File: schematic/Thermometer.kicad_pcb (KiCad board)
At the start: 2 copper layers, 55.4 x 52.8 mm, 18 parts, among them Q1 BC547, Q2 BC547, Q3 BC547, Q4 BC547, SW1 SW_SPDT, U1 CC56-12EWA, U2 DS18B20, U3 DS18B20

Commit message: Updated Schematic and PCB with (hopefully) final designs
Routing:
- net Net-(Q3-B): track 53.3 -> 77.8 mm, vias 2 -> 3
- net Net-(SW1-C): track 96.7 -> 115.0 mm, vias 1 -> 2
- net Net-(Q2-B): track 74.0 -> 57.0 mm, vias 2 -> 1
- net Net-(Q1-E): track 51.7 -> 42.5 mm
- net Net-(A1-A1): track 67.0 -> 59.1 mm
- net Net-(A1-D11): track 47.8 -> 54.9 mm
- net Net-(Q3-C): track 55.3 -> 48.4 mm
- net Net-(A1-D9): track 45.7 -> 50.8 mm
- net Net-(A1-D2): track 27.5 -> 22.6 mm
- net Net-(A1-D12): track 42.7 -> 47.3 mm
- net Net-(Q2-C): track 39.9 -> 44.1 mm
- net Net-(A1-+5V): track 85.7 -> 82.3 mm, vias 0 -> 1
- net Net-(D1-K): track 48.3 -> 51.6 mm
- net Net-(A1-D3): track 24.7 -> 21.9 mm, vias 0 -> 1
- net Net-(U2-DQ): track 34.4 -> 36.5 mm, vias 0 -> 1
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
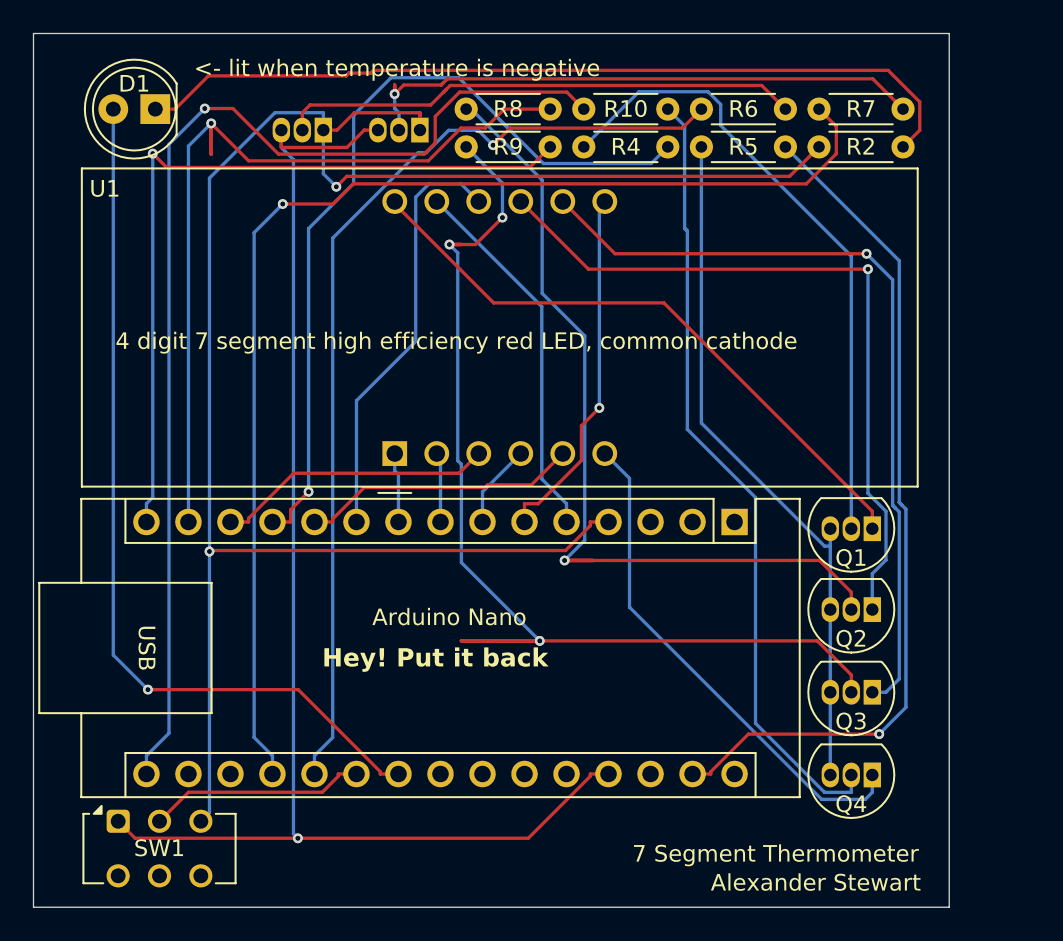
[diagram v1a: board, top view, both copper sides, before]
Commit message: Updated error in PCB design
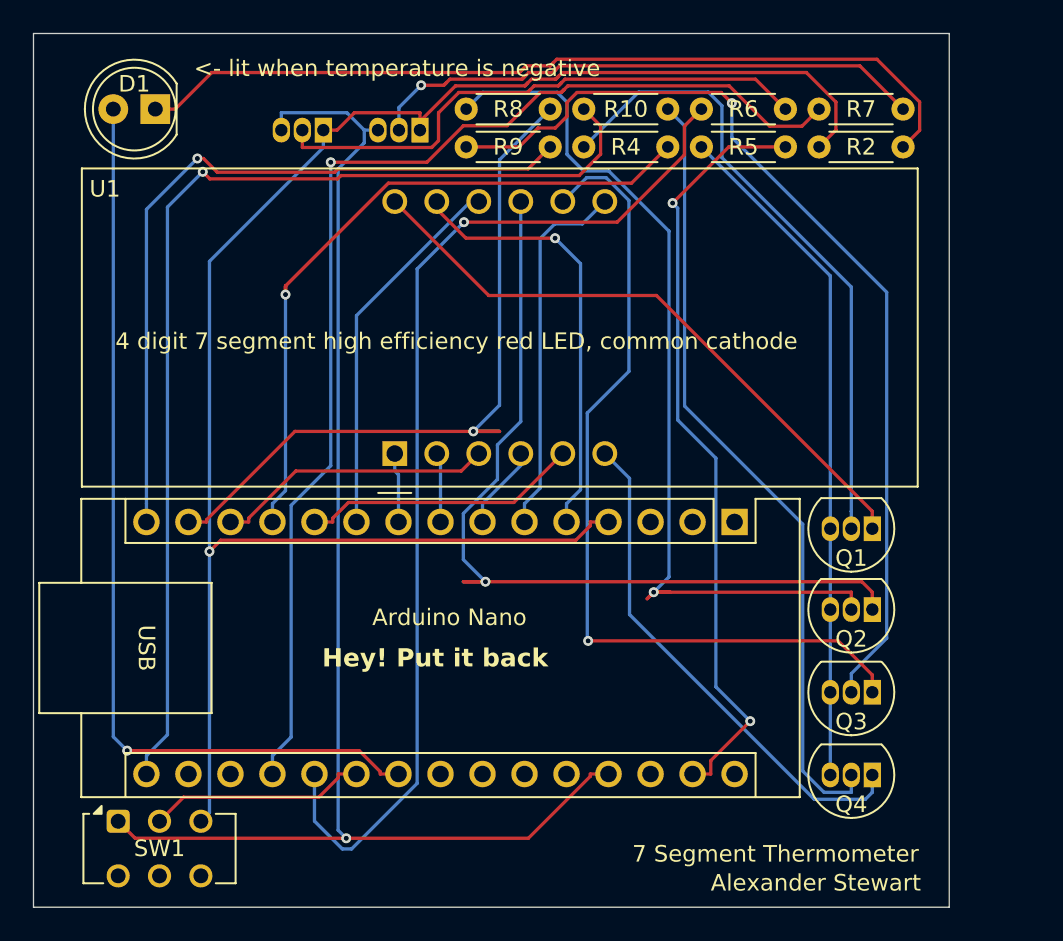
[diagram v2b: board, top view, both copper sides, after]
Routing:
- net Net-(Q3-B): track 77.8 -> 58.6 mm, vias 3 -> 1
- net Net-(Q2-C): track 44.1 -> 55.0 mm
- net Net-(A1-D11): track 54.9 -> 47.3 mm
- net Net-(A1-D9): track 50.8 -> 43.3 mm
- net Net-(SW1-C): track 115.0 -> 107.9 mm, vias 2 -> 1
- net Net-(A1-A1): track 59.1 -> 64.7 mm
- net Net-(A1-GND-Pad29): track 51.8 -> 46.8 mm, vias 1 -> 2
- net Net-(A1-D2): track 22.6 -> 26.5 mm, vias 0 -> 1
- net Net-(Q3-C): track 48.4 -> 52.2 mm
- net Net-(A1-D7): track 25.7 -> 22.7 mm
- net Net-(A1-A3): track 53.3 -> 56.2 mm
- net Net-(A1-D13): track 68.7 -> 65.8 mm
- net Net-(U3-DQ): track 31.8 -> 34.2 mm
- net Net-(A1-A0): track 73.5 -> 71.6 mm
- net Net-(U2-DQ): track 36.5 -> 34.6 mm
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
